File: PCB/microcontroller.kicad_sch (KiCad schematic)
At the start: 27 parts, among them IC1 STM32F479VGT6, X1 7P-26.000MBP-T

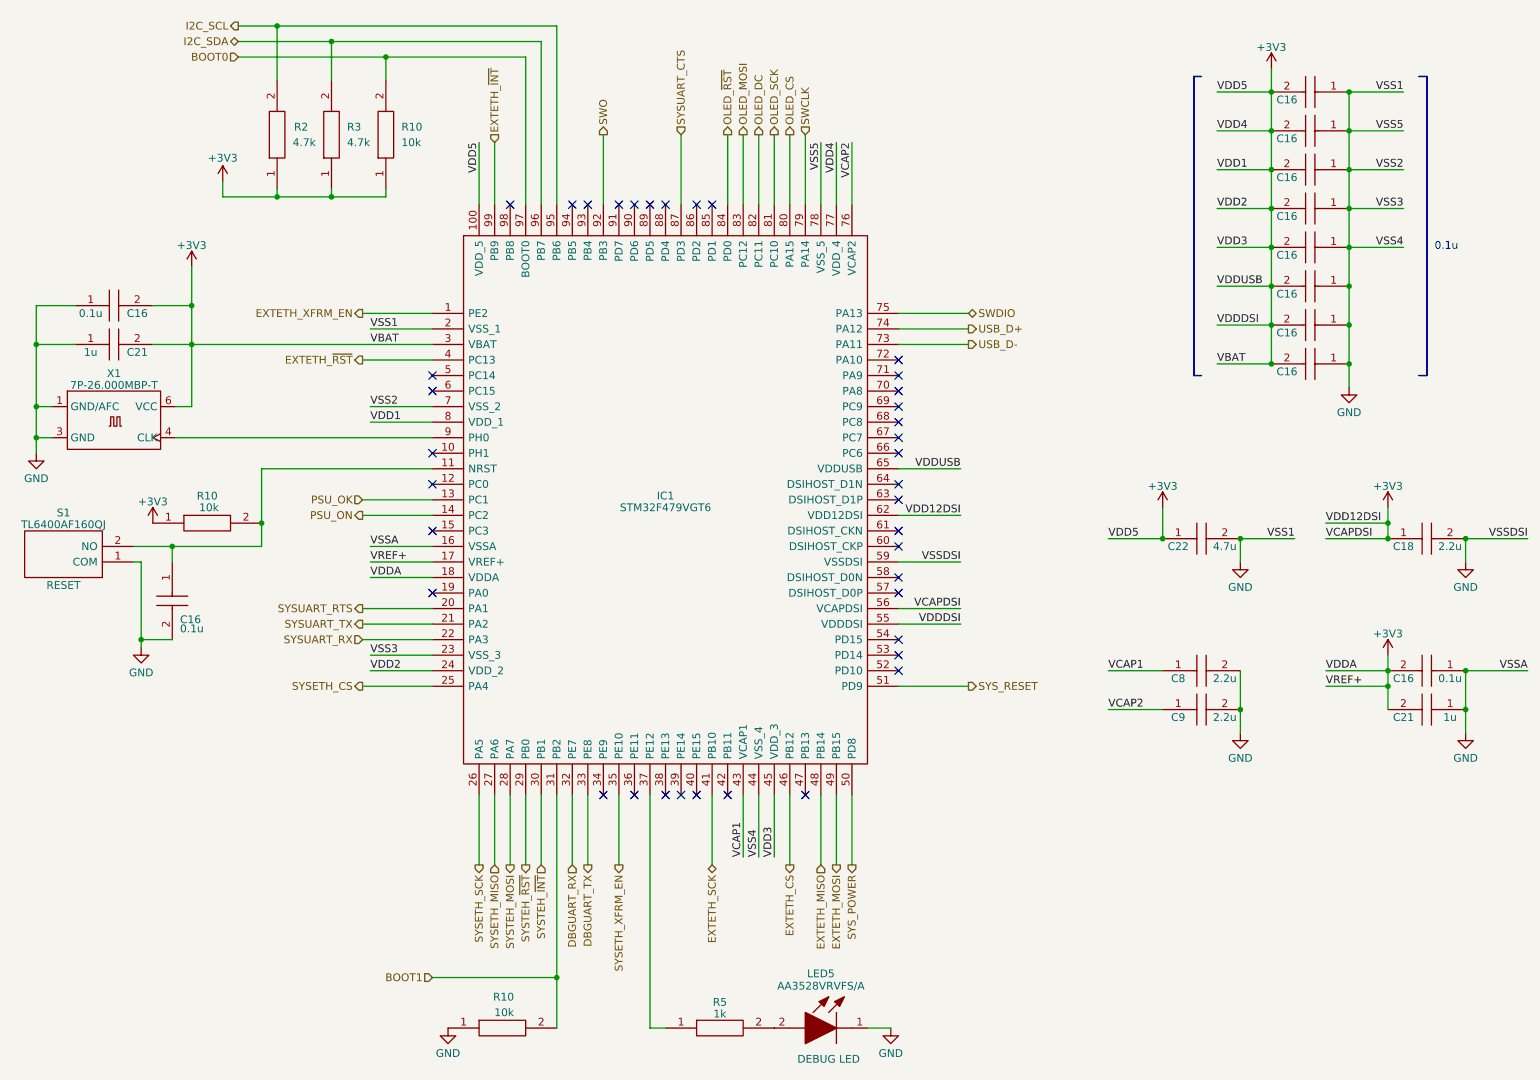
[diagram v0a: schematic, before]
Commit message: redo pinout of entire MCU (closes #34)
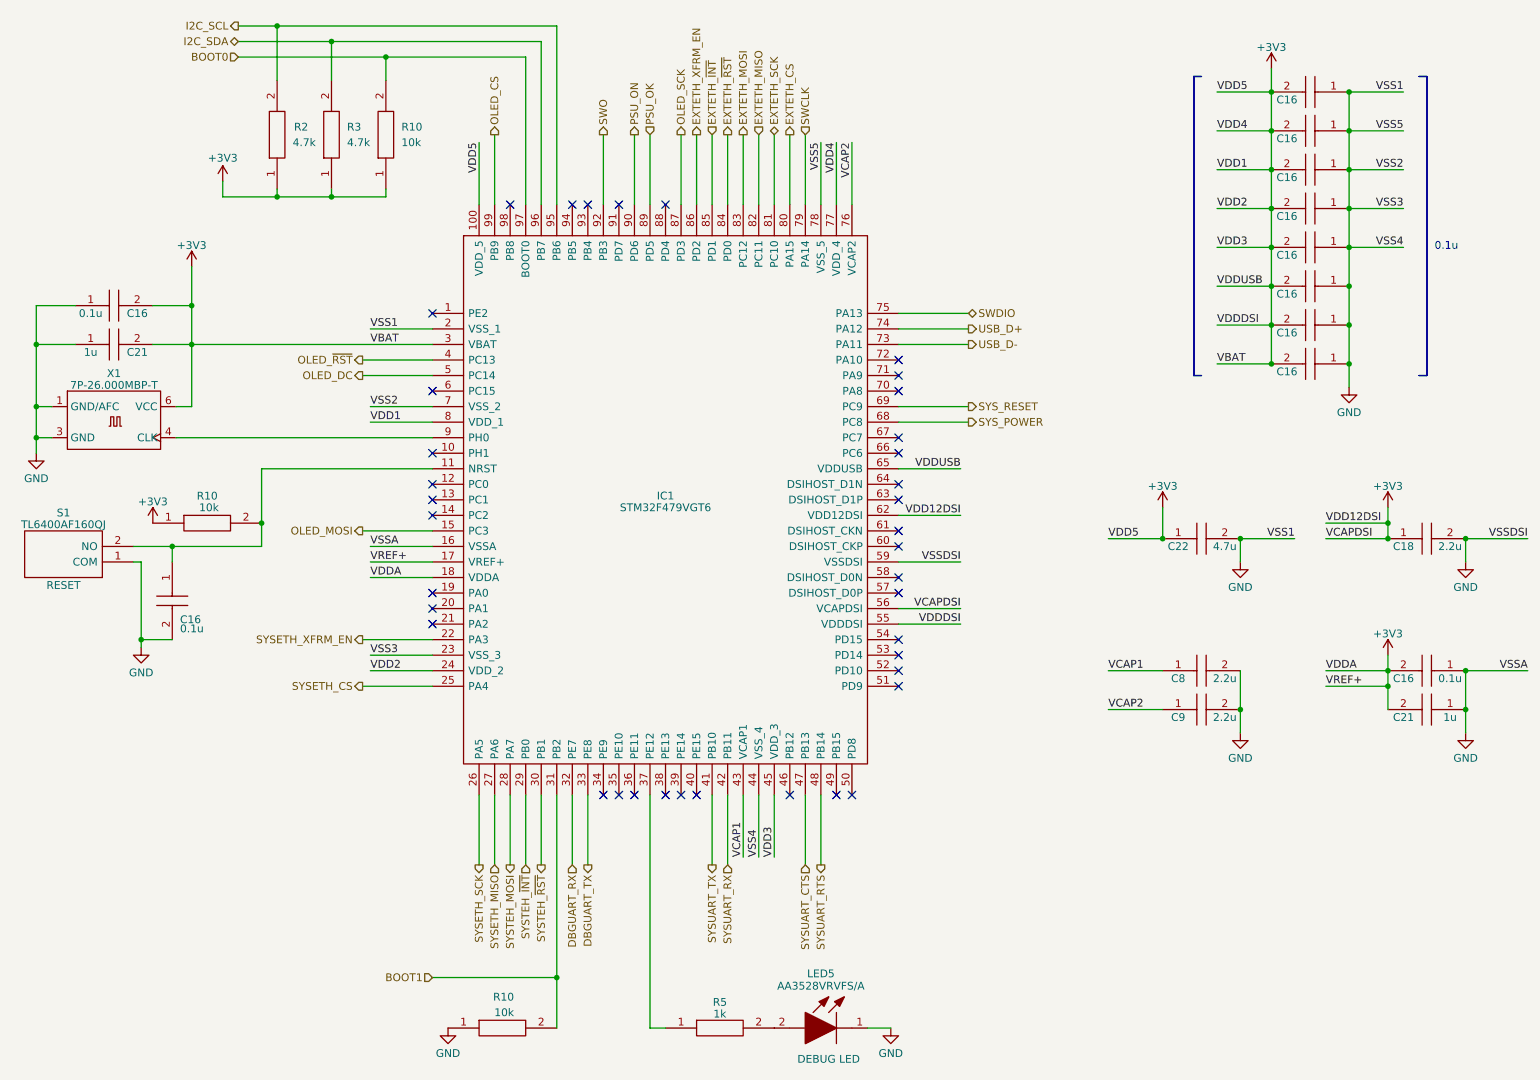
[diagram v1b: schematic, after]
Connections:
- net EXTETH_CS: now also IC1.80 (PA15); no longer IC1.46 (PB12)
- net EXTETH_MISO: now also IC1.82 (PC11); no longer IC1.48 (PB14)
- net EXTETH_MOSI: now also IC1.83 (PC12); no longer IC1.49 (PB15)
- net EXTETH_SCK: now also IC1.81 (PC10); no longer IC1.41 (PB10)
- net EXTETH_XFRM_EN: now also IC1.86 (PD2); no longer IC1.1 (PE2)
- net EXTETH_~{INT}: now also IC1.85 (PD1); no longer IC1.99 (PB9)
- net EXTETH_~{RST}: now also IC1.84 (PD0); no longer IC1.4 (PC13)
- net OLED_CS: now also IC1.99 (PB9); no longer IC1.80 (PA15)
- net OLED_DC: now also IC1.5 (PC14); no longer IC1.82 (PC11)
- net OLED_MOSI: now also IC1.15 (PC3); no longer IC1.83 (PC12)
- net OLED_SCK: now also IC1.87 (PD3); no longer IC1.81 (PC10)
- net OLED_~{RST}: now also IC1.4 (PC13); no longer IC1.84 (PD0)
- net PSU_OK: now also IC1.89 (PD5); no longer IC1.13 (PC1)
- net PSU_ON: now also IC1.90 (PD6); no longer IC1.14 (PC2)
- net SYSETH_XFRM_EN: now also IC1.22 (PA3); no longer IC1.35 (PE10)
- net SYSTEH_~{INT}: now also IC1.29 (PB0); no longer IC1.30 (PB1)
- net SYSTEH_~{RST}: now also IC1.30 (PB1); no longer IC1.29 (PB0)
- net SYSUART_CTS: now also IC1.47 (PB13); no longer IC1.87 (PD3)
- net SYSUART_RTS: now also IC1.48 (PB14); no longer IC1.20 (PA1)
- net SYSUART_RX: now also IC1.42 (PB11); no longer IC1.22 (PA3)
- net SYSUART_TX: now also IC1.41 (PB10); no longer IC1.21 (PA2)
- net SYS_POWER: now also IC1.68 (PC8); no longer IC1.50 (PD8)
- net SYS_RESET: now also IC1.69 (PC9); no longer IC1.51 (PD9)

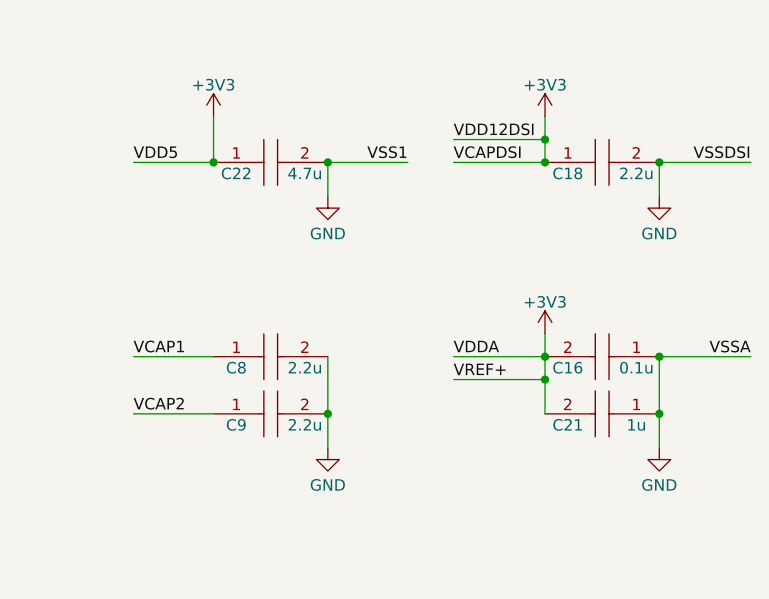
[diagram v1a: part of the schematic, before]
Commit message: silkscreen, via, and comment polishing
This isn't the change for the following issues, which were all addressed
over the last few commits, collectively. Sorry for the messiness.

Closes #30
Closes #26
Closes #25
Closes #9
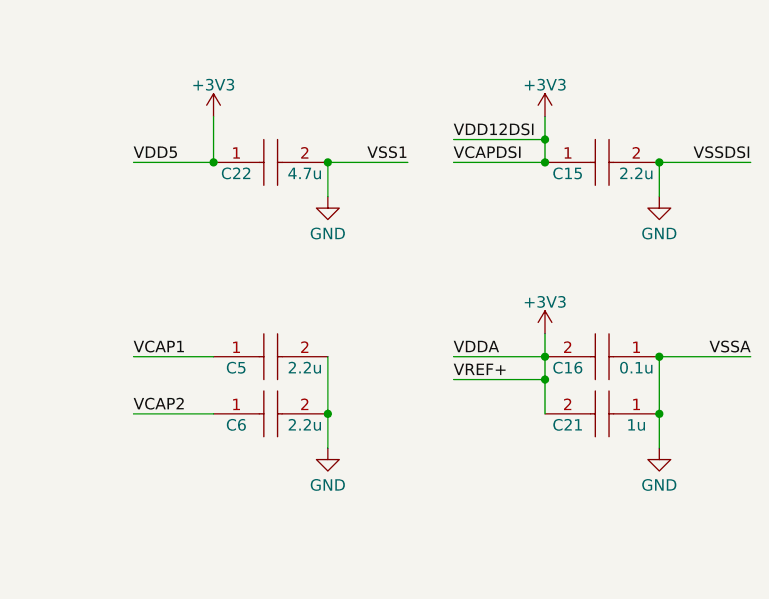
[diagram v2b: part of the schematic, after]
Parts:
- renumbered C18 to C15, C8 to C5, C9 to C6

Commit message: fix mouser ID on MSAST1L3YB5104KFNA01 caps
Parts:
- C16: symbol SamacSys_Parts:MSAST1L3YB5104KFNA01 -> Oro:MSAST1L3YB5104KFNA01; Mouser Part Number (none) -> 963-MSAST1L3YB5104KF; Mouser Price/Stock (none) -> https://www.mouser.de/ProductDetail/TAIYO-YUDEN/MSAST1L3YB5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

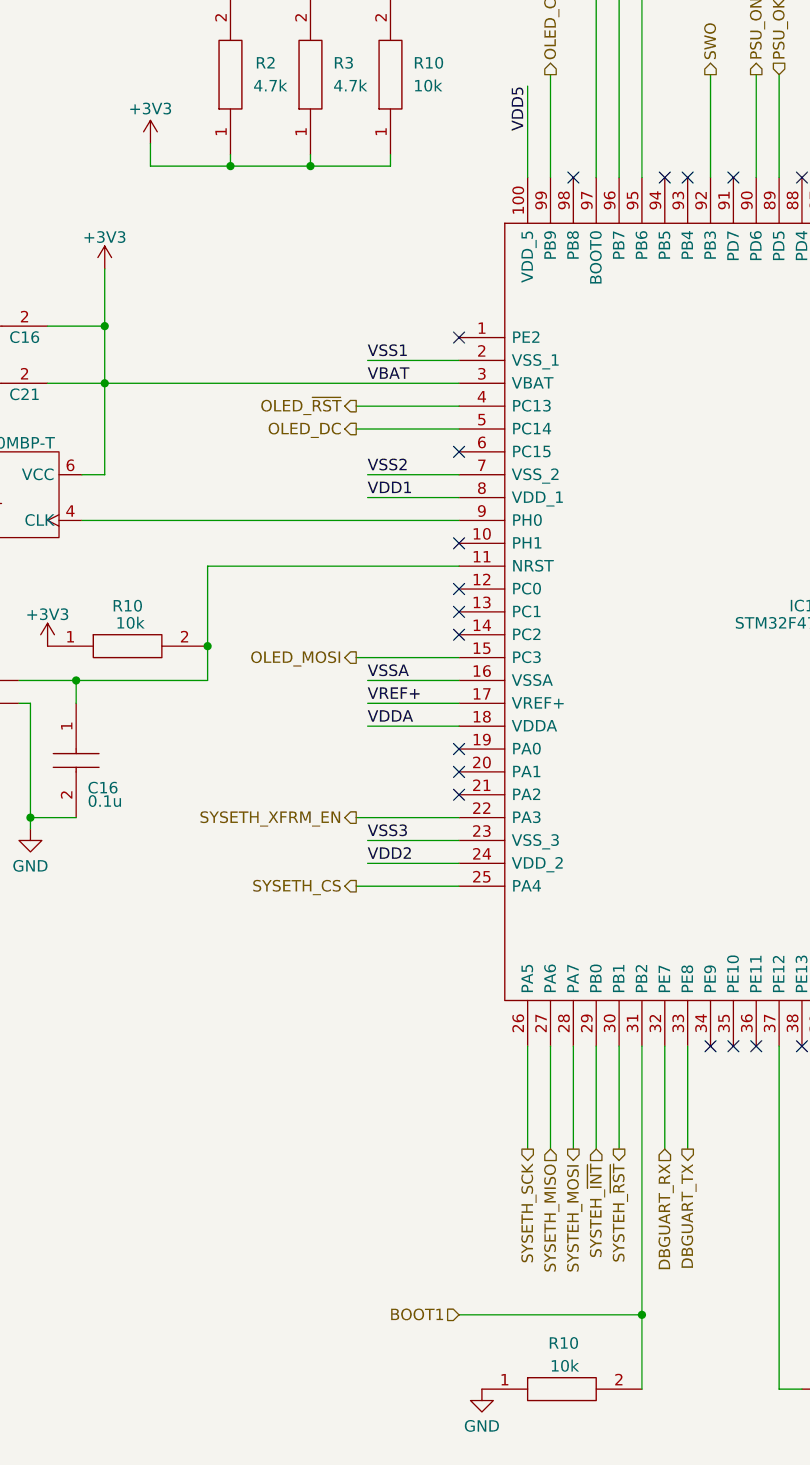
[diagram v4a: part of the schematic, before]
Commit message: reverse BOOT0/BOOT1 pull-up/-down resistor configuration (fixes #41)
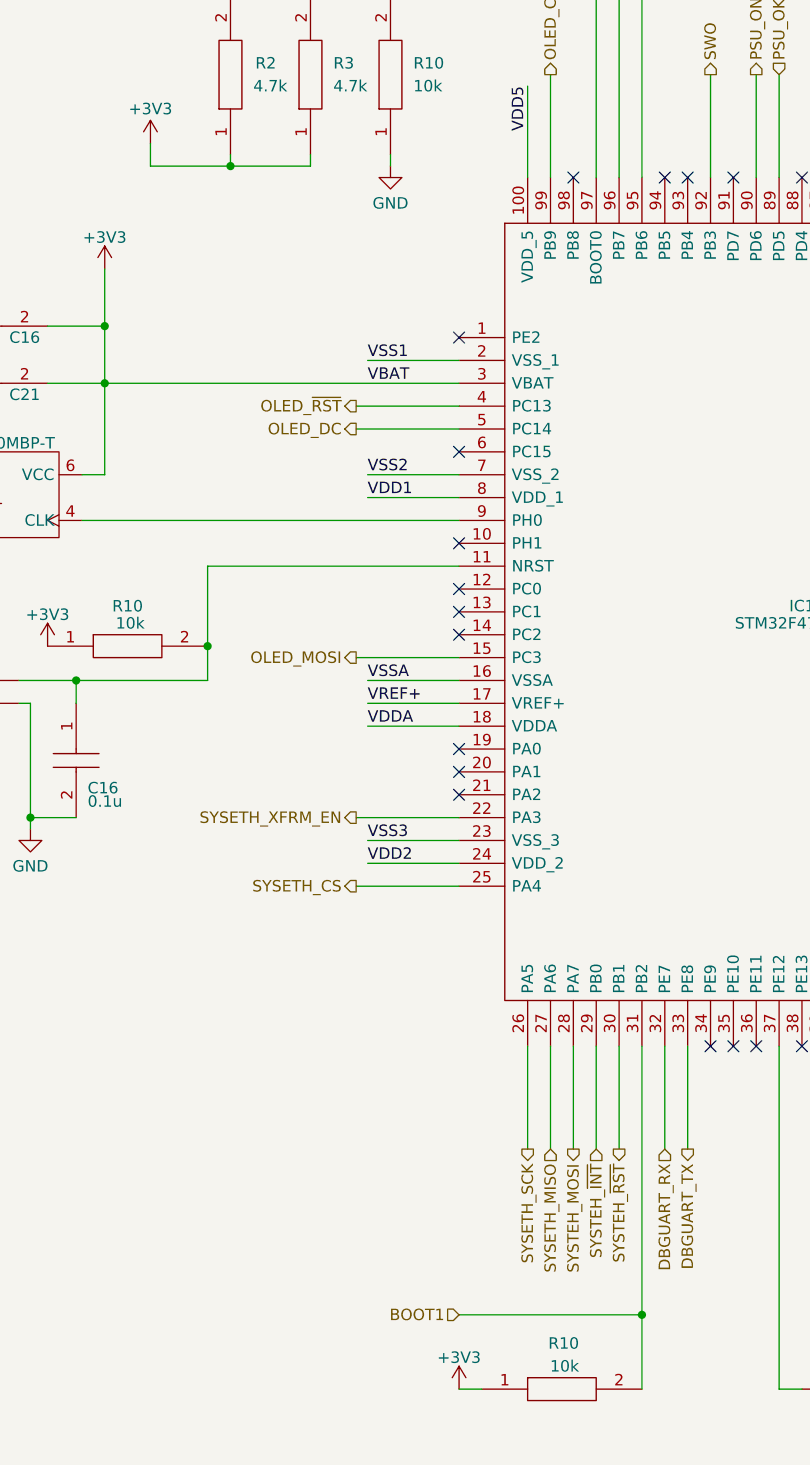
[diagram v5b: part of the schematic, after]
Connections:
- net +3V3: now also R10.1; no longer R10.1
- net GND: now also R10.1; no longer R10.1
